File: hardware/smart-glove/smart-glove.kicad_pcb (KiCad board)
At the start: 2 copper layers, 50 x 40 mm, 5 parts, among them J2 FLEX

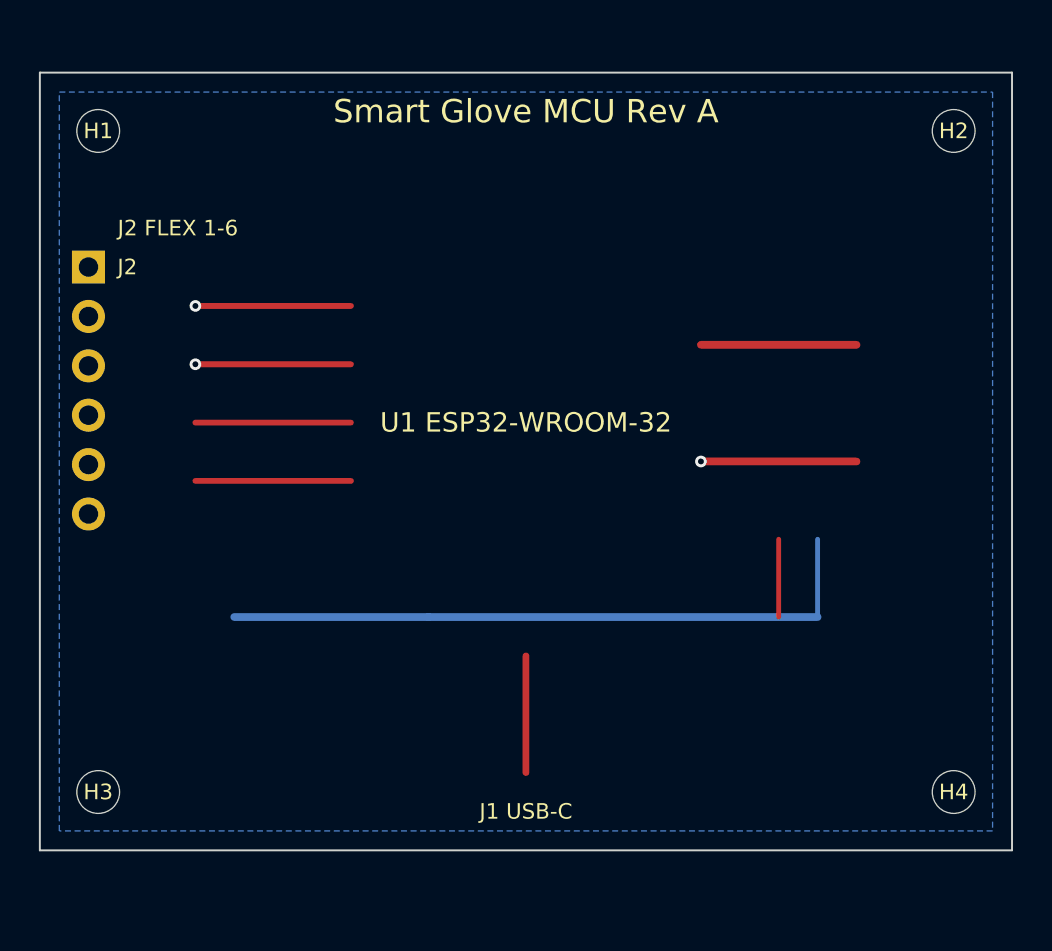
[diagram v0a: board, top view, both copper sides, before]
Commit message: Make Smart Glove PCB fab-ready for prototype production
Generate a complete KiCad 7 board with library footprints (ESP32-WROOM-32,
TP4056, AMS1117, MPU-6050, USB-C, passives), nets, routing, and GND copper.

Export JLCPCB package: Gerbers, Excellon drill, BOM, CPL, fabrication notes,
production board preview, and automated design-check report.

Co-authored-by: ADIL ZAHOOR  <adilzahoor2812@users.noreply.github.com>
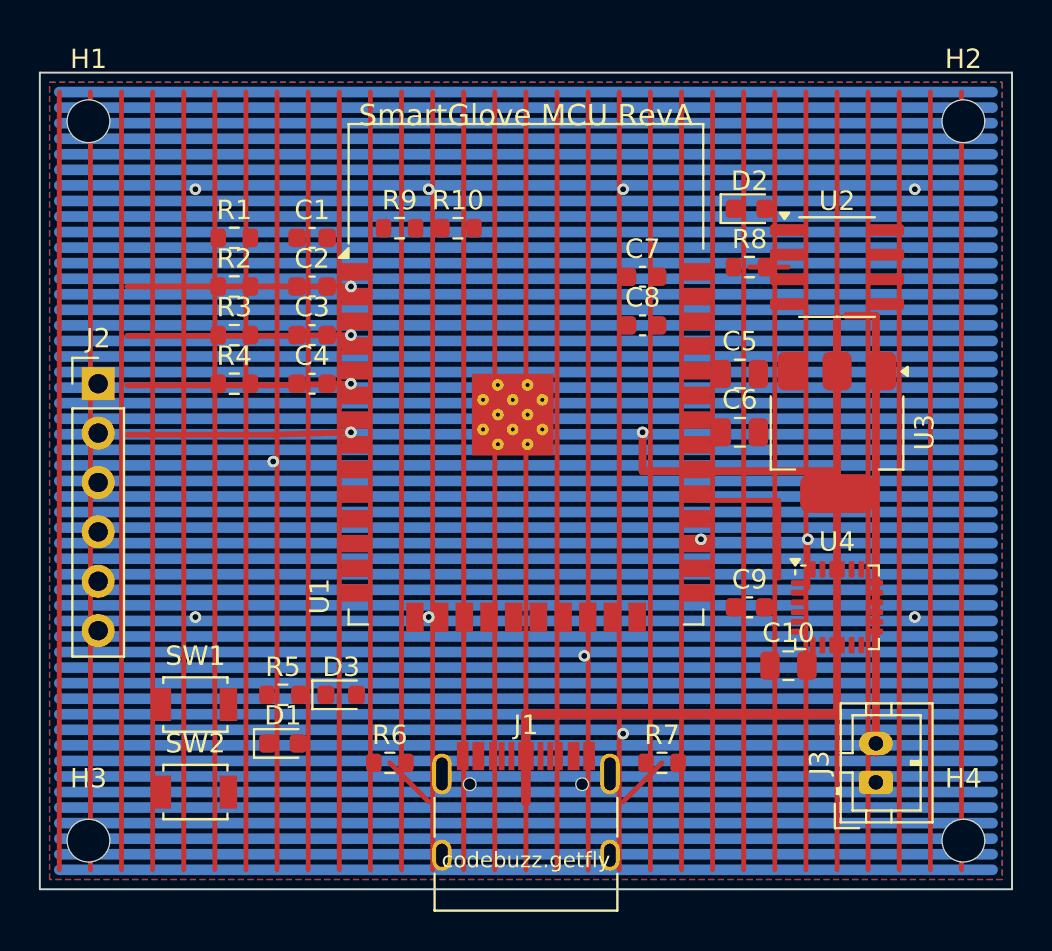
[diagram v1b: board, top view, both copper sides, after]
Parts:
- added C1: 100nF, C_0603_1608Metric, F.Cu at (14.0, 8.50)
- added C10: 2.2uF, C_0805_2012Metric, F.Cu at (38.5, 30.5)
- added C2: 100nF, C_0603_1608Metric, F.Cu at (14.0, 11.0)
- added C3: 100nF, C_0603_1608Metric, F.Cu at (14.0, 13.5)
- added C4: 100nF, C_0603_1608Metric, F.Cu at (14.0, 16.0)
- added C5: 10uF, C_0805_2012Metric, F.Cu at (36.0, 15.5)
- added C6: 22uF, C_0805_2012Metric, F.Cu at (36.0, 18.5)
- added C7: 100nF, C_0603_1608Metric, F.Cu at (31.0, 10.5)
- added C8: 100nF, C_0603_1608Metric, F.Cu at (31.0, 13.0)
- added C9: 100nF, C_0603_1608Metric, F.Cu at (36.5, 27.5)
- added D1: LED-PWR, LED_0603_1608Metric, F.Cu at (12.5, 34.5)
- added D2: LED-CHRG, LED_0603_1608Metric, F.Cu at (36.5, 7.00)
- added D3: LED-STAT, LED_0603_1608Metric, F.Cu at (15.5, 32.0)
- added J1: USB-C, USB_C_Receptacle_HRO_TYPE-C-31-M-12, F.Cu at (25.0, 39.2)
- added J3: LiPo, JST_PH_B2B-PH-K_1x02_P2.00mm_Vertical, F.Cu at (43.0, 36.5)
- added R1: 10k, R_0603_1608Metric, F.Cu at (10.0, 8.50)
- added R10: 10k, R_0603_1608Metric, F.Cu at (21.5, 8.00)
- added R2: 10k, R_0603_1608Metric, F.Cu at (10.0, 11.0)
- added R3: 10k, R_0603_1608Metric, F.Cu at (10.0, 13.5)
- added R4: 10k, R_0603_1608Metric, F.Cu at (10.0, 16.0)
- added R5: 1k, R_0603_1608Metric, F.Cu at (12.5, 32.0)
- added R6: 5.1k, R_0603_1608Metric, F.Cu at (18.0, 35.5)
- added R7: 5.1k, R_0603_1608Metric, F.Cu at (32.0, 35.5)
- added R8: 1.2k, R_0603_1608Metric, F.Cu at (36.5, 10.0)
- added R9: 10k, R_0603_1608Metric, F.Cu at (18.5, 8.00)
- added SW1: BOOT, SW_SPST_B3U-1000P, F.Cu at (8.00, 32.5)
- added SW2: EN/RST, SW_SPST_B3U-1000P, F.Cu at (8.00, 37.0)
- added U1: ESP32-WROOM-32E, ESP32-WROOM-32, F.Cu at (25.0, 18.5)
- added U2: TP4056, SOIC-8_3.9x4.9mm_P1.27mm, F.Cu at (41.0, 10.0)
- added U3: AMS1117-3.3, SOT-223, F.Cu at (41.0, 18.5)
- added U4: MPU-6050, InvenSense_QFN-24_4x4mm_P0.5mm, F.Cu at (41.0, 27.5)
- H1, H2, H3, H4: footprint MountingHole:MountingHole_2.2mm_M2 -> MountingHole_2.2mm_M2
- J2: footprint Connector_PinHeader_2.54mm:PinHeader_1x06_P2.54mm_Vertical -> PinHeader_1x06_P2.54mm_Vertical
- moved J2 6.02 mm to (3.00, 16.0), turned to 0 degrees
- moved H3 2.55 mm to (2.50, 39.5)
- moved H4 2.55 mm to (47.5, 39.5)
- moved H1 0.71 mm to (2.50, 2.50)
- moved H2 0.71 mm to (47.5, 2.50)
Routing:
- net GND: track 38.0 -> 3648.0 mm, vias 1 -> 10
- net +5V: track 6.00 -> 40.7 mm
- net +BAT: track 0.00 -> 28.0 mm
- net SDA: track 4.00 -> 8.00 mm
- net SCL: track 4.00 -> 8.00 mm, vias 0 -> 2
- net 3V3: track 8.00 -> 12.0 mm, vias 0 -> 1
- net FLEX4: track 8.00 -> 11.5 mm, vias 0 -> 1
- net FLEX3: track 8.00 -> 11.5 mm, vias 0 -> 1
- net FLEX2: track 8.00 -> 11.5 mm
- net FLEX1: track 8.00 -> 11.5 mm
- net CC2: track 0.00 -> 2.83 mm
- net CC1: track 0.00 -> 2.83 mm
- net TP_PROG: track 0.00 -> 2.00 mm
- added copper zone on F.Cu, net GND
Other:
- board size 50 x 40 mm -> 50 x 42 mm
- board text added: "SmartGlove MCU RevA"
- board text added: "codebuzz.getfly"
- board text removed: "J1 USB-C"
- board text removed: "J2 FLEX 1-6"
- board text removed: "Smart Glove MCU Rev A"
- board text removed: "U1 ESP32-WROOM-32"

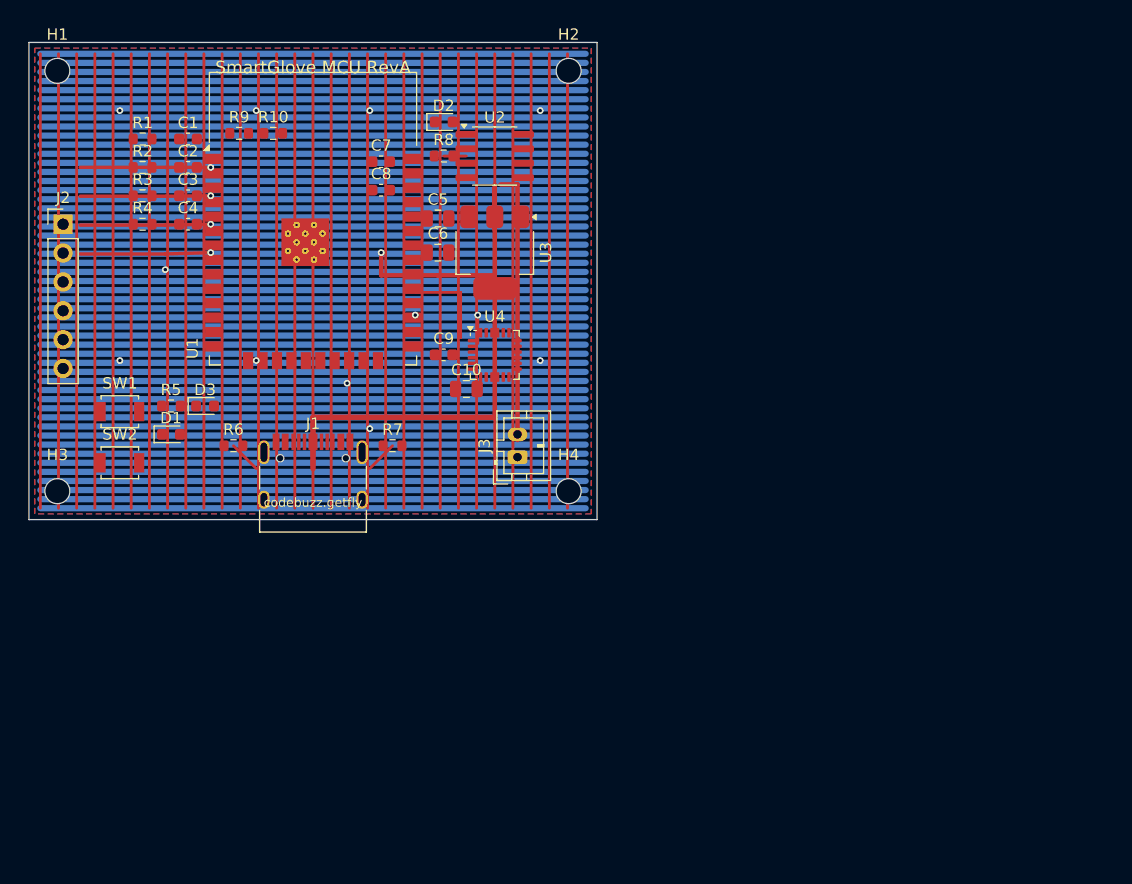
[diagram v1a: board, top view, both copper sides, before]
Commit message: Compile ERC and DRC reports with KiCad 8 CLI
Run official sch erc and pcb drc on the Smart Glove project and save
text/json reports plus a compile summary under fab/.

Co-authored-by: ADIL ZAHOOR  <adilzahoor2812@users.noreply.github.com>
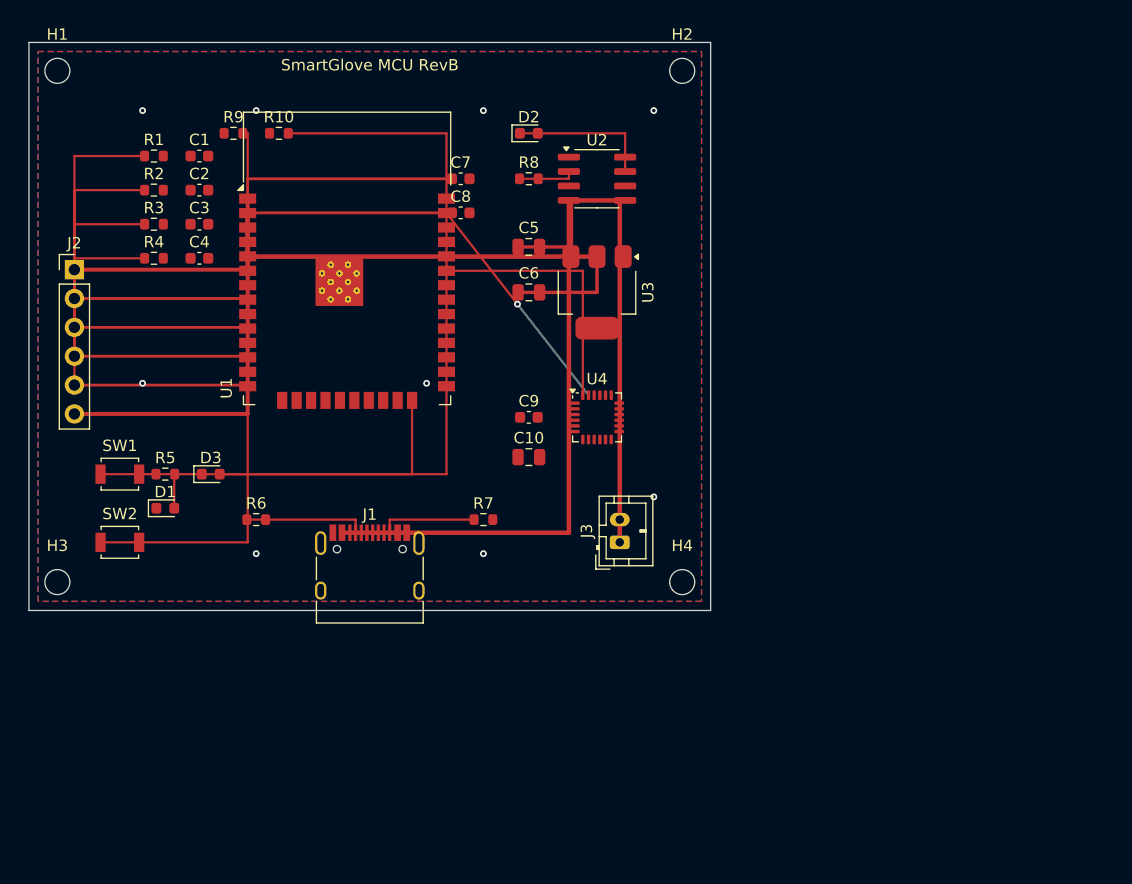
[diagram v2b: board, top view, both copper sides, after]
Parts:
- SW2: value EN/RST -> EN
- moved H4 12.8 mm to (57.5, 47.5)
- moved J3 11.7 mm to (52.0, 44.0)
- moved U4 10.5 mm to (50.0, 33.0)
- moved R7 10.3 mm to (40.0, 42.0)
- moved H2 10.0 mm to (57.5, 2.50)
- moved U3 9.66 mm to (50.0, 22.0)
- moved J1 9.43 mm to (30.0, 47.2)
- moved C9 9.30 mm to (44.0, 33.0)
- moved U2 9.22 mm to (50.0, 12.0)
- moved C6 8.73 mm to (44.0, 22.0)
- moved C5 8.38 mm to (44.0, 18.0)
- moved C10 8.14 mm to (44.0, 36.5)
- moved H3 8.00 mm to (2.50, 47.5)
- moved R8 7.76 mm to (44.0, 12.0)
- moved D2 7.57 mm to (44.0, 8.00)
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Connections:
- U2 pad 6: GND -> (no net)
- U4 pad 20: GND -> (no net)
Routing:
- net GND: track 3648.0 -> 34.2 mm, vias 10 -> 9
- net 3V3: track 12.0 -> 103.9 mm, vias 1 -> 0
- net BOOT: track 0.00 -> 74.4 mm
- net EN: track 0.00 -> 49.4 mm
- net FLEX4: track 11.5 -> 41.4 mm, vias 1 -> 0
- net FLEX3: track 11.5 -> 40.6 mm, vias 1 -> 0
- net FLEX2: track 11.5 -> 39.8 mm, vias 1 -> 0
- net FLEX1: track 11.5 -> 38.9 mm, vias 1 -> 0
- net STAT_LED: track 0.00 -> 23.4 mm
- net +BAT: track 28.0 -> 45.8 mm
- net SDA: track 8.00 -> 22.9 mm
- net CHRG: track 0.00 -> 12.6 mm
- net SCL: track 8.00 -> 20.3 mm, vias 2 -> 1
- net +5V: track 40.7 -> 49.2 mm
- net CC1: track 2.83 -> 10.7 mm
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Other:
- board size 50 x 42 mm -> 60 x 50 mm
- board text added: "SmartGlove MCU RevB"
- board text removed: "RF KEEP-OUT"
- board text removed: "SmartGlove MCU RevA"
- board text removed: "codebuzz.getfly"

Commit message: Make Smart Glove MCU PCB production-ready (Rev D)
Autoroute with Freerouting after clean placement, pour GND on both
layers, and ship a fab package that passes ERC/DRC with zero
unconnected nets (95×72 mm, JLCPCB-oriented).

Co-authored-by: ADIL ZAHOOR  <adilzahoor2812@users.noreply.github.com>
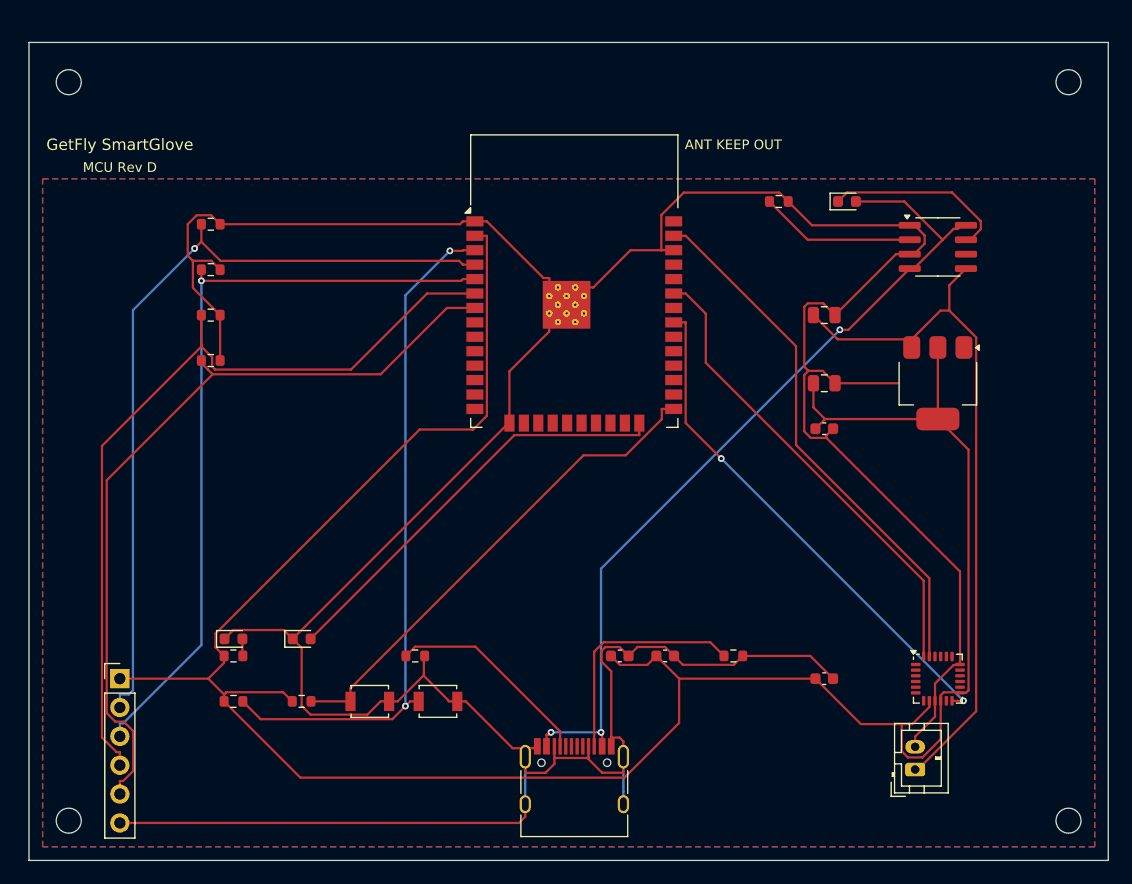
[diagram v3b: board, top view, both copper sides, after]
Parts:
- removed C10: 2.2uF, C_0805_2012Metric
- removed C3, C4, C8: 100nF, C_0603_1608Metric
- moved C2 58.0 mm to (56.0, 54.0)
- moved C1 57.5 mm to (52.0, 54.0)
- moved R10 50.0 mm to (24.0, 58.0)
- moved R9 50.0 mm to (18.0, 58.0)
- moved H4 40.0 mm to (91.5, 68.5)
- moved C7 38.8 mm to (70.0, 34.0)
- moved U4 37.8 mm to (80.0, 56.0)
- moved J2 36.2 mm to (8.00, 56.0)
- moved C9 34.7 mm to (70.0, 56.0)
- moved H2 34.0 mm to (91.5, 3.50)
- moved J3 32.8 mm to (78.0, 64.0)
- moved SW2 31.3 mm to (36.0, 58.0)
- moved U3 31.0 mm to (80.0, 30.0)
- moved U2 30.6 mm to (80.0, 18.0)
- moved SW1 29.7 mm to (30.0, 58.0)
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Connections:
- J1 pad : GND -> (no net)
- J1 pad A6: USB_DP -> (no net)
- J1 pad A7: USB_DN -> (no net)
- J1 pad B6: USB_DP -> (no net)
- J1 pad B7: USB_DN -> (no net)
- U1 pad 34: USB_DN -> (no net)
- U1 pad 35: USB_DP -> (no net)
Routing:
- net GND: track 34.2 -> 348.3 mm, vias 9 -> 0
- net 3V3: track 103.9 -> 210.6 mm
- net IMU_INT: track 0.00 -> 45.5 mm, vias 0 -> 2
- net FLEX1: track 38.9 -> 70.9 mm, vias 0 -> 1
- net FLEX3: track 40.6 -> 72.2 mm
- net BOOT: track 74.4 -> 43.8 mm
- net FLEX4: track 41.4 -> 70.0 mm
- net FLEX2: track 39.8 -> 68.4 mm, vias 0 -> 1
- net SCL: track 20.3 -> 47.0 mm, vias 1 -> 0
- net +5V: track 49.2 -> 75.3 mm, vias 0 -> 3
- net SDA: track 22.9 -> 41.7 mm
- net +BAT: track 45.8 -> 62.7 mm
- net STAT_LED: track 23.4 -> 37.4 mm
- net CC2: track 8.58 -> 20.6 mm
- net EN: track 49.4 -> 60.7 mm, vias 0 -> 2
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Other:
- board size 60 x 50 mm -> 95 x 72 mm
- board text added: "ANT KEEP OUT"
- board text added: "GetFly SmartGlove"
- board text added: "MCU Rev D"
- board text removed: "SmartGlove MCU RevB"

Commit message: Align Rev D PCB with complete schematic; DRC/ERC clean
PCB now matches the full schematic: SCL on U1.36, REGOUT+C10,
USB SBU NC. Rebuild gate passes — ERC 0 errors, DRC 0, unconnected 0.

Co-authored-by: ADIL ZAHOOR  <adilzahoor2812@users.noreply.github.com>
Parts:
- added C10: 2.2uF, C_0805_2012Metric, F.Cu at (70.0, 50.0)
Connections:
- J1 pad A8: GND -> (no net)
- J1 pad B8: GND -> (no net)
- U1 pad 36: GND -> SCL
- U1 pad 37: SCL -> (no net)
- U1 pad 38: (no net) -> GND
- U4 pad 10: 3V3 -> REGOUT
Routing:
- net GND: track 348.3 -> 316.2 mm
- net REGOUT: track 0.00 -> 18.7 mm
- net FLEX3: track 72.2 -> 89.2 mm
- net FLEX1: track 70.9 -> 87.7 mm, vias 1 -> 0
- net IMU_INT: track 45.5 -> 53.0 mm, vias 2 -> 0
- net 3V3: track 210.6 -> 204.0 mm, vias 0 -> 4
- net +5V: track 75.3 -> 78.1 mm, vias 3 -> 2
- net CC2: track 20.6 -> 18.6 mm
- net CC1: track 18.3 -> 20.1 mm, vias 0 -> 2
- net SCL: track 47.0 -> 45.7 mm
- net +BAT: track 62.7 -> 61.6 mm, vias 0 -> 1
- net EN: track 60.7 -> 60.0 mm, vias 2 -> 3
- net FLEX4: track 70.0 -> 70.7 mm
- net TP_PROG: track 13.7 -> 14.4 mm

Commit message: Build SignSpeak Smart Glove Rev E fab package (5 flex)
PCB/schematic branded Man Who Embed; J2 1x7 with FLEX1-5.
Production gate: ERC 0 errors, DRC 0, unconnected 0.

Co-authored-by: ADIL ZAHOOR  <adilzahoor2812@users.noreply.github.com>
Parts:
- added R11: 10k, R_0603_1608Metric, F.Cu at (16.0, 32.0)
- J2: footprint PinHeader_1x06_P2.54mm_Vertical -> PinHeader_1x07_P2.54mm_Vertical
- moved J2 6.00 mm to (8.00, 50.0)
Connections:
- J2 pad 6: GND -> FLEX5
- U1 pad 8: (no net) -> FLEX5
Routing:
- net FLEX5: track 0.00 -> 62.7 mm
- net EN: track 60.0 -> 90.2 mm, vias 3 -> 0
- net GND: track 316.2 -> 343.7 mm, vias 0 -> 2
- net FLEX3: track 89.2 -> 62.4 mm, vias 0 -> 1
- net FLEX1: track 87.7 -> 64.9 mm, vias 0 -> 1
- net +5V: track 78.1 -> 99.8 mm, vias 2 -> 0
- net 3V3: track 204.0 -> 190.6 mm, vias 4 -> 0
- net IMU_INT: track 53.0 -> 46.2 mm, vias 0 -> 2
- net FLEX4: track 70.7 -> 64.4 mm, vias 0 -> 1
- net FLEX2: track 68.2 -> 62.2 mm
- net +BAT: track 61.6 -> 57.8 mm
- net REGOUT: track 18.7 -> 16.7 mm, vias 0 -> 2
- net CC2: track 18.6 -> 20.2 mm, vias 0 -> 2
- net CC1: track 20.1 -> 19.3 mm
- net TP_PROG: track 14.4 -> 13.7 mm
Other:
- board text added: "Man Who Embed Rev E"
- board text added: "SignSpeak Smart Glove"
- board text removed: "GetFly SmartGlove"
- board text removed: "MCU Rev D"
